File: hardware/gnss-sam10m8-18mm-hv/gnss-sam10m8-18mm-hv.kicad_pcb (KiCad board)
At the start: 4 copper layers, 22 x 27.5 mm, 29 parts, among them J3 BM05B-SRSS-TB, U1 SAM-M10Q-00B, U3 TPS62913RPUR

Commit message: hardware: battery protection, boost swap, and a capacitor voltage audit
Base station power chain, all verified against exported netlists:

- Protection: MAX17303G+ gauge/protector and its NTMD6N02R2G FET pair
  replaced by DW01A + 2x FS8205A. The MAX17303 had no firmware driver and
  the board never had a working coulomb counter, so state of charge already
  came from the voltage curve in bs_battery_soc.h; it now reads a 1M/1M
  divider on GPIO1. The FETs move from the positive rail to the negative
  one because the DW01A has no charge pump, so board ground is now P-,
  separated from the cell's B- by the FET stack. Two FS8205A in parallel
  put the 150 mV overcurrent trip at ~4.8-6.0 A instead of ~2.4-3.0 A.
  TH1 moves onto the BQ21040's TS pin, replacing a fixed 10k that had been
  defeating thermal charge cutoff.

- V_LORA retargeted 7.49 V -> 4.95 V and LM5157QRTERQ1 -> TPS61023DRLR.
  Nothing needed 7.4 V (everything downstream is 3.3 V behind the
  TPS62913), while an RFD868x-class radio is 5 V nominal with a 6 V
  absolute maximum, so the old rail put it permanently out of reach. Being
  synchronous and internally compensated also dropped D2, C35-C38 and R10.
  Inductor stays the fleet 2.2 uH: inside TI's 0.37-2.9 uH range and the
  only value meeting their ripple-under-40%-of-average guidance at load.

- Keystone 1043P holder -> MYOUNG BH-18650-A5BJ001-2D. Terminal pitch
  72.30 vs 72.22 mm, so the battery nets did not move; BT2 is rotated 180
  degrees because this part's positive end is mirrored.

Across all four boards:

- Every crystal was mis-loaded. 32.768 kHz parts saw ~9 pF against a 6 pF
  spec and the 40 MHz saw 12.5 pF against 10 pF, both pulling slow. Moved
  to Seiko SC-32S (12.5 pF) with 22 pF load caps, and the 40 MHz caps to
  18 pF. The tolerance being paid for had been swamped several times over.

- Capacitor voltage audit, new Min V rating column in the BOM. Three parts
  were operating outside their rating on 8.4 V rails: 47 uF and 100 u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
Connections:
- U3 pad 10: GND -> Net-(U3-EN/SYNC)
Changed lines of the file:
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@@
 			(layers "F.Cu" "F.Mask" "F.Paste")
 			(roundrect_rratio 0.025)
-			(net "GND")
+			(net "Net-(U3-EN{slash}SYNC)")
 			(pinfunction "S-CONF_10")
 			(pintype "output")

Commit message: hardware: gnss board placement tidy, and populate J3
J3 (BM05B-SRSS-TB) loses its DNP attribute and will now be populated.

8 parts repositioned: the three 22 uF bulk caps C1/C12/C14 line up in a
row at y=40.24, and C5, C6, FB1 and L8 move with them. +7 track
segments, +1 via.

Co-Authored-By: Claude Opus 5 <noreply@anthropic.com>
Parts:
- moved C14 10.4 mm to (58.5, 40.2), turned to -90 degrees
- moved C6 3.81 mm to (62.9, 37.9), turned to 0 degrees
- moved FB1 2.36 mm to (59.7, 37.5)
- moved C5 2.26 mm to (62.9, 37.0), turned to 0 degrees
- moved L8 1.53 mm to (54.0, 43.0), turned to 90 degrees
- moved C12 1.17 mm to (60.4, 40.2)
- moved C1 1.14 mm to (62.4, 40.2)
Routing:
- net +3V3: track 4.89 -> 6.56 mm
- net Net-(U3-EN/SYNC): track 1.57 -> 2.31 mm
- net GND: vias 47 -> 48

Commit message: hardware: single-source each board's version through the title block
Every board hardcoded its marketing version inside a silkscreen gr_text
("LoRa V3", "Tinker\nRocket\nV9", ...), where it could drift from the git
tag with nothing to catch it.

The version token now lives in the PCB title block as (rev "V3") and the
silkscreen references ${REVISION}. KiCad resolves that at plot time,
including from kicad-cli, so the artwork is unchanged -- verified by
plotting F.SilkS + B.SilkS for all five boards before and after and
comparing stroke counts:

  lora-daughterboard      260 -> 260
  rocket-computer        1236 -> 1236
  base-station            687 -> 687
  gnss-sam10m8-18mm-hv    366 -> 366
  gnss-px1105r-...        353 -> 353

Four changed lines per board and nothing else. servo-adapter is untouched
-- it carries no version on silkscreen yet.

Co-Authored-By: Claude Opus 5 <noreply@anthropic.com>
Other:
- board text added: "TinkerRocket GNSS SAM-M10Q ${REVISION}"
- board text removed: "TinkerRocket GNSS SAM-M10Q V2"
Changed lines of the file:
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@@
 	)
 	(paper "A4")
+	(title_block
+		(rev "V2")
+	)
 	(layers
 		(0 "F.Cu" signal)
@@
 		)
 	)
-	(gr_text "TinkerRocket\nGNSS SAM-M10Q\nV2"
+	(gr_text "TinkerRocket\nGNSS SAM-M10Q\n${REVISION}"
 		(at 53.15 43.29 0)
 		(layer "B.SilkS")

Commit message: hardware: declare filled+capped vias on the 6-layer boards; in-progress board edits
Two separate things, kept together because they land in the same board files.

1. Via protection, mine.  lora-daughterboard and rocket-computer both place
   vias in pads, and the fab fills those on 6-layer stackups -- but the board
   files still declared (filling no) (capping no), so nothing in the exported
   data said so.  Both now declare IPC-4761 Type VII (filled and capped),
   which is the process via-in-pad actually requires.  base-station is left at
   (filling no) (capping no): it is 4-layer and does not get the treatment.

2. In-progress layout work, the user's, carried along in the same files:

   rocket-computer  J7 removed (superseded by the J8 JST VH battery inlet);
                    C20/C22/C48/C49 crystal caps 18 pF -> 12 pF now reflected
                    in copper; 8 parts flipped side, 23 repositioned, routing
                    and via count adjusted to suit
   lora-daughterboard  routing and ground stitching (+8 vias, +10 segments)
   base-station     one via removed
   gnss-sam10m8-18mm-hv       C15 added; C11/C13 47 uF -> 22 uF
   gnss-px1105r-...-ext-ant   C16/R8/R9 added; C13/C14 47 uF -> 22 uF

The 47 -> 22 uF swap on both GNSS boards is already reflected in the
cross-board BOM: the 47 uF line is now rocket-computer only (1), and 22 uF
GNSS went 5 -> 8.

Co-Authored-By: Claude Opus 5 <noreply@anthropic.com>
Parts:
- added C15: 22 uF, Capacitor_SMD:C_0805_2012Metric, F.Cu at (50.6, 37.0)
- added R7: 1 k, Resistor_SMD:R_0402_1005Metric, F.Cu at (47.3, 38.4)
- added R8: 1 k, Resistor_SMD:R_0402_1005Metric, F.Cu at (47.3, 40.3)
- C11, C13: value 47 uF -> 22 uF
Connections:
- J3 pad 1: GNSS_RX -> Net-(J3-Pad1)
- J3 pad 2: GNSS_TX -> Net-(J3-Pad2)
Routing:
- net +3V3: vias 8 -> 7

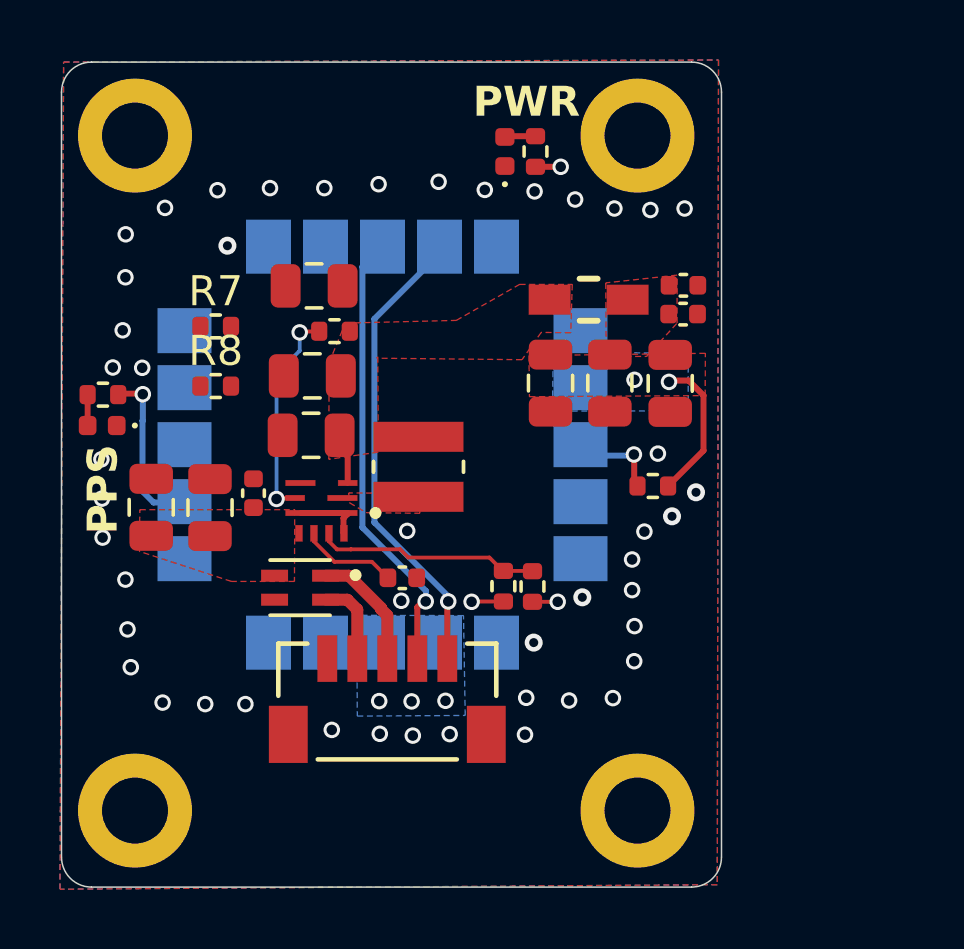
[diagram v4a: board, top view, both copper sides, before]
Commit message: hardware(gnss-sam10m8): JLC 4-layer stackup + ENIG, and land the CR1/R7-R8 work
Two things in one commit because the board file carried both.

Inherited: the .kicad_pcb was already modified relative to main before this
branch started, and the 2026-08-04 pre-manufacturing review was written against
that state, not against main. Recording it here so the review and the file agree:
  - CR1 (SMF10A) added, VSYS -> GND at (46.105, 48.740). Not present on main.
  - R7/R8 relocated from the left edge to beside J3, with GNSS_TX/GNSS_RX
    re-routed through them (hence Net-(J3-Pad1)/Net-(J3-Pad2)).
  - C10 moved and NR/SS + FB re-routed. This is what introduced the FB segment
    at y=44.890 running x 52.689 -> 55.600 that review finding A2 is about.

Stackup (review C6): copper_finish None -> ENIG and the real JLC 4-layer
profile, matching what lora-daughterboard and base-station already got. ENIG
matters here specifically because the SAM-M10Q is a 20-pad LGA and HASL's domed
pads hurt coplanarity and standoff on flat-pad packages.

Worth noting the modelled dielectric changes with it: prepreg was described as
0.1 mm and is really 0.2104 mm, so F.Cu -> In1.Cu is twice as far as the review
assumed. Nothing was designed to the old number, but it does weaken the "In1 is
close enough to limit lateral coupling" argument in A2 and B7 -- both of which
are being fixed anyway.

DRC unchanged: 9 warnings (4 lib_footprint_mismatch, 5 silk_over_copper),
0 unconnected, 0 schematic-parity issues.

Co-Authored-By: Claude Opus 5 <noreply@anthropic.com>
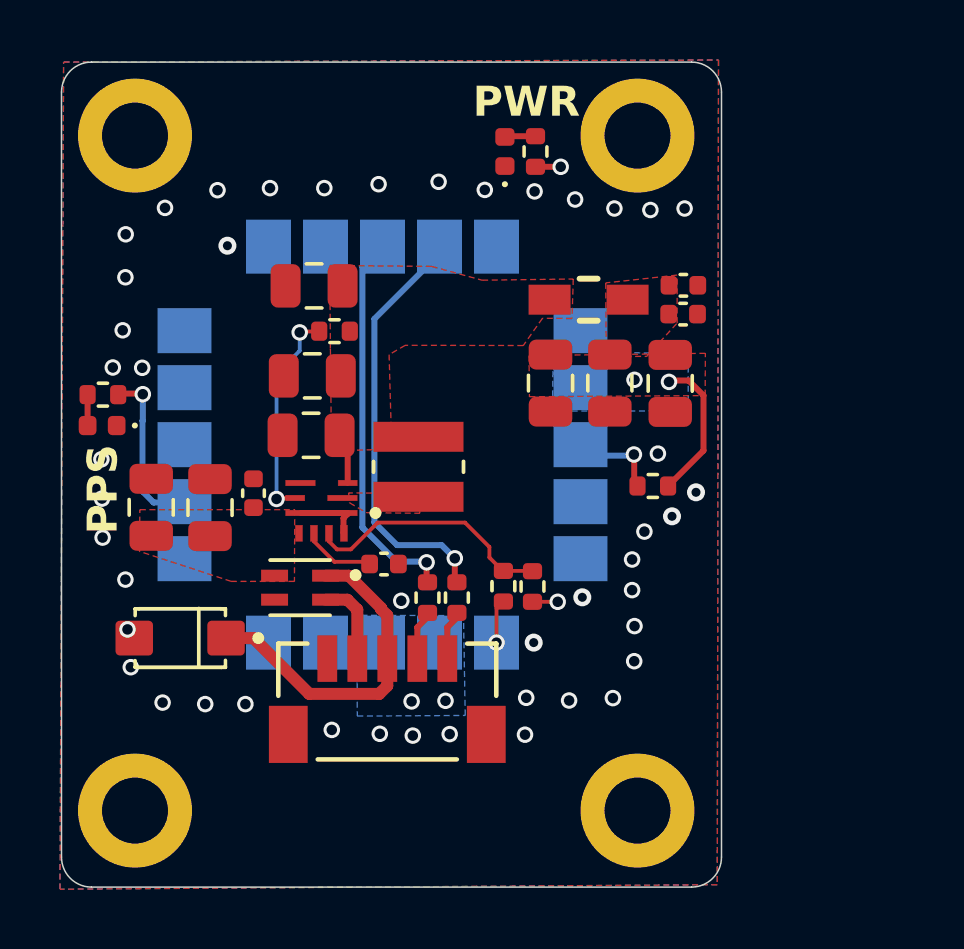
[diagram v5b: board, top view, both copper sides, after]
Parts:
- added CR1: SMF10A, Footprints:SODFL3617X108N, F.Cu at (46.1, 48.7)
- D1, D3: value LED -> Green
- moved R7 12.1 mm to (55.3, 47.4), turned to -90 degrees
- moved R8 9.98 mm to (54.4, 47.4), turned to -90 degrees
- moved C10 0.76 mm to (52.9, 46.3)
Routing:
- net VSYS: track 4.07 -> 11.2 mm
- net GNSS_TX: track 15.7 -> 13.0 mm
- net Net-(J3-Pad2): track 0.00 -> 2.28 mm
- net Net-(J3-Pad1): track 0.00 -> 1.66 mm
- net GNSS_RX: track 15.9 -> 14.3 mm
- net Net-(U3-FB): track 7.53 -> 8.47 mm
- net Net-(U3-NR/SS): track 3.24 -> 2.44 mm
- net GND: track 1.06 -> 1.47 mm, vias 48 -> 47
- net +3V3: vias 7 -> 6

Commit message: hardware(gnss-sam10m8): pre-fab fixes -- TVS path, PSNS via, module stitching, PPS
Acts on the 2026-08-04 pre-manufacturing review. DRC after: 10 warnings
(5 lib_footprint_mismatch, 5 silk_over_copper), 0 unconnected items,
0 schematic-parity issues. Baseline was 9/0/0; the extra footprint mismatch is
R9 inheriting R2's library drift and is resolved separately.

A3 -- PSNS and PGND now have ground vias. TI SLVSFP4B 10.1 requires PSNS tied
to the plane with a via, and PSNS has the tightest absolute maximum on the part
(-0.3/+0.3 V). A via centred on the pad is not manufacturable here: U3's pads
are on a 0.5 mm pitch, leaving 0.248 mm between pad edges, so a via with 0.2 mm
clearance would need to be 0.34 mm -- below JLC's minimum. Both vias sit just
off the pad instead (0.15 mm for PSNS, 0.10 mm for PGND) on a short stub.

A4 -- V_BCKP left open per u-blox 4.1.3, with a no-connect flag. Also
no-connects on SAFEBOOT_N, SDA, SCL, EXTINT and PG, so ERC can tell deliberate
from forgotten. This removed 7 of the 11 ERC errors; the remaining 4 are
pre-existing power_pin_not_driven.

B1 -- CR1 moved from (46.105, 48.740) to (52.510, 54.665), under the connector,
and its anode moved from GND to VSS. The clamp path was
J3.3 -> CR1 -> GND -> FL1 winding 3-4 -> VSS -> J3.4, which put the choke's
common-mode impedance in the middle of the clamp and risked the part (320 mA
rating vs the SMF10A's 11.8 A). VSYS and VSS now run straight down from J3.3
and J3.4 as a 1 mm-spaced pair, so the transient loop is local and tightly
coupled. Note this is 5.24 mm from the connector rather than adjacent -- J3's
own courtyard is the binding constraint and no closer position exists in any
orientation.

B2 -- 11 GND vias added under the module (u-blox 4.4 asks for the plane below
it to be filled with vias); there were 5. Four more were generated but landed
inside the VO and +3V3 zone fills and were dropped.

B4 -- H1-H4 mounting pads assigned to GND. They were 3.8 mm of netless floating
copper on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
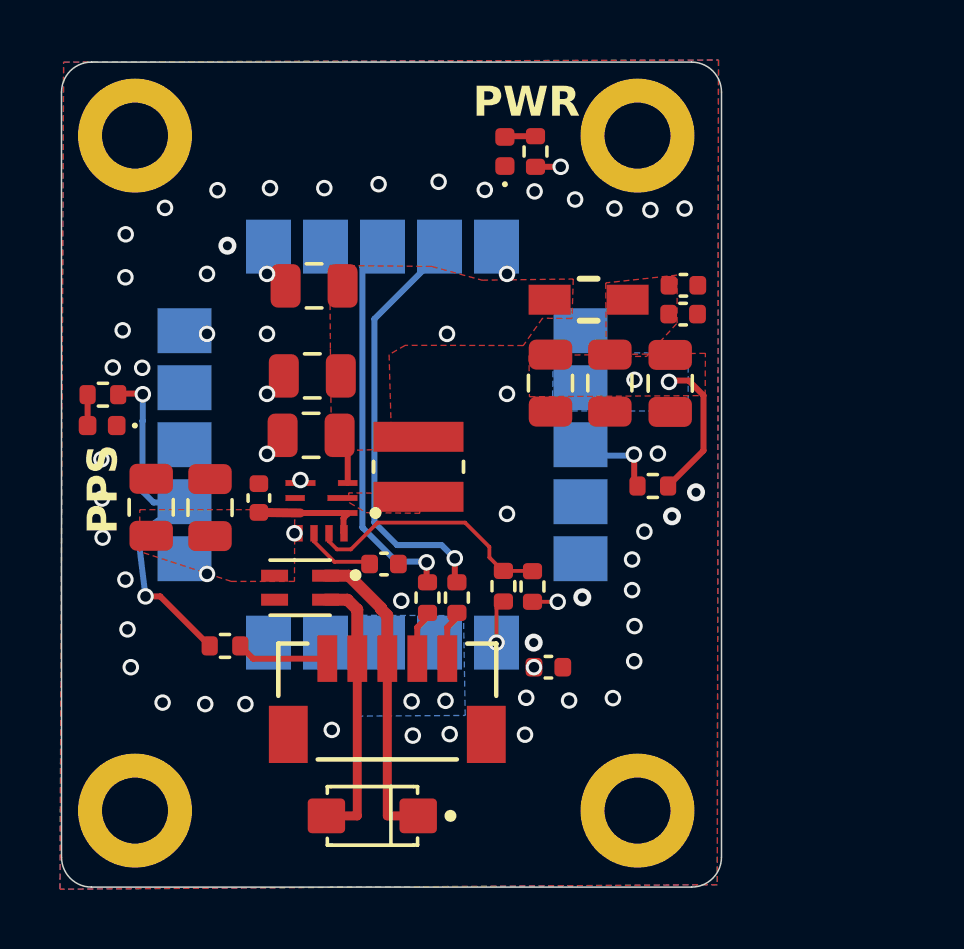
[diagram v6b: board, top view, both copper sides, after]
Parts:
- removed R4: 10 k, Resistor_SMD:R_0402_1005Metric
- added C16: 100 nF, Capacitor_SMD:C_0402_1005Metric, F.Cu at (58.4, 49.7)
- added R9: 1 k, Resistor_SMD:R_0402_1005Metric, F.Cu at (47.6, 49.0)
- moved CR1 8.73 mm to (52.5, 54.7)
- moved C7 0.24 mm to (48.7, 44.1)
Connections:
- net Net-(U1-TIMEPULSE) renamed PPS
- CR1 pad A: GND -> VSS
- H1 pad 1: (no net) -> GND
- H2 pad 1: (no net) -> GND
- H3 pad 1: (no net) -> GND
- H4 pad 1: (no net) -> GND
- J3 pad 5: RXD2 -> Net-(J3-Pad5)
- J3 pad 6: (no net) -> GND
- J3 pad 7: (no net) -> GND
- U1 pad 3: +3V3 -> unconnected-(U1-V_BCKP-Pad3)
- U3 pad 5: Net-(U3-PG) -> unconnected-(U3-PG-Pad5)
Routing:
- net Net-(U3-PG): track 7.18 -> 0.00 mm, vias 2 -> 0
- net PPS: track 5.66 -> 12.5 mm, vias 1 -> 2
- net VSS: track 2.83 -> 9.10 mm
- net Net-(J3-Pad5): track 0.00 -> 3.08 mm
- net Net-(U3-EN/SYNC): track 2.31 -> 3.70 mm
- net VSYS: track 11.2 -> 10.3 mm
- net GND: track 1.47 -> 1.72 mm, vias 47 -> 59
- net +3V3: vias 6 -> 7

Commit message: hardware(gnss-sam10m8): bom.csv pinning the two capacitor groups that cannot float
Review finding A1. No capacitor on this board carried an MPN and there was no
bom.csv, so the assembler picked the part. For most of the board that is fine.
Two groups it is not, and both were hidden inside one "22 uF 0805" line:

C8, C9 (VIN bulk) -- changed 22 uF -> 10 uF and pinned to a 25 V X7S part.
VIN is raw pack voltage: 7.4 V nominal, 8.4 V on a fully charged 2S, and CR1
does not begin clamping until 11.1 V. The default 22 uF 0805 at every
distributor and in JLC's basic library is 6.3 V or 10 V rated, so the board as
drawn could have been built with parts operated over their rating. 2 x 10 uF
25 V is TI's own reference value for CIN (SLVSFP4B), clears the 5 uF effective
minimum after DC-bias derating, and halves hot-plug inrush versus 2 x 22 uF.
The schematic and footprint values are updated to match so parity holds.

C11, C13, C15 (first-stage COUT) -- pinned to TDK C2012X7S1A226M125AC. TI
specifies a 40-80 uF EFFECTIVE window at 3.33 V bias, not a minimum, because
the loop compensation is internal and non-adjustable. A common 22 uF 0805
6.3 V X5R derates to ~10-12 uF each: three of them give 30-36 uF, below the
minimum, with nothing on the board to indicate it. The X7S part holds
~15-16 uF each, ~46 uF total.

The remaining lines carry the constraints that are load-bearing but invisible
in a value: CR1 must not be substituted with SMF12A (19.9 V clamp would exceed
the TPS62913's 18 V absolute maximum); D1 must stay a green LED because its
forward drop is the only thing holding TIMEPULSE/SAFEBOOT_N out of the safeboot
window at startup; C7 needs a >=25 V rating.

DRC unchanged: 10 warnings, 0 unconnected, 0 schematic-parity issues.

Co-Authored-By: Claude Opus 5 <noreply@anthropic.com>
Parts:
- C8, C9: value 22 uF -> 10 uF
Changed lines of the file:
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@@
 			)
 		)
-		(property "Value" "22 uF"
+		(property "Value" "10 uF"
 			(at 0 1.68 90)
 			(layer "F.Fab")
@@
 			)
 		)
-		(property "Value" "22 uF"
+		(property "Value" "10 uF"
 			(at 0 1.68 90)
 			(layer "F.Fab")
